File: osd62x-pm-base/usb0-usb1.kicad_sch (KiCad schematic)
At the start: 1 part

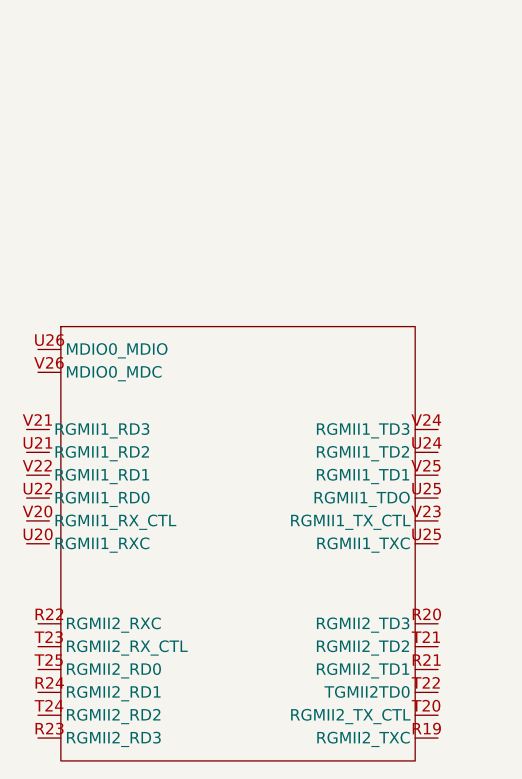
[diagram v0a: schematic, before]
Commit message: Unit F created and placed.
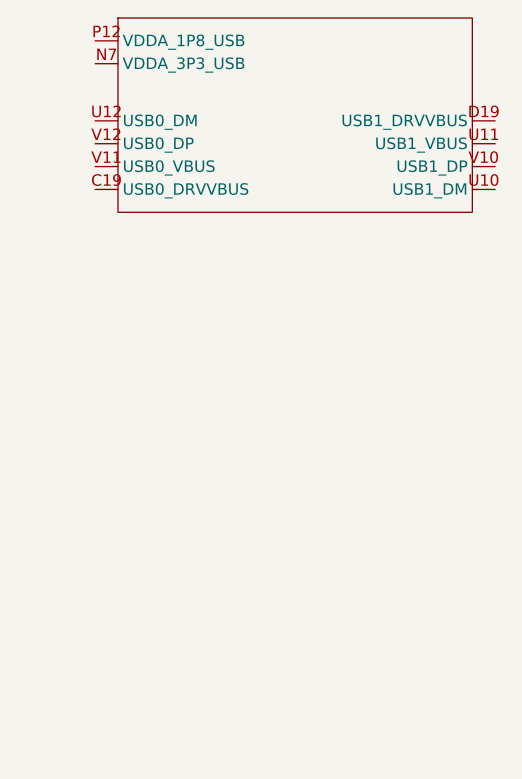
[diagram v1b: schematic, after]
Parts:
- removed U1: ~, symbol octavo_Library:osd62x-pm
- added U1: ~, symbol octavo_Library:osd62x-pm
